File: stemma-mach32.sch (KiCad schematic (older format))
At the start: 28 parts, among them J1 Conn_01x09_Male, J2 Conn_01x04_Male, J3 Conn_01x04_Male, J4 Conn_01x09_Male, J5 DebugEdge_02x04, Q1 BSS138, Q2 BSS138, U1 AP2112K-3.3, U2 MACHXO2-32QFN

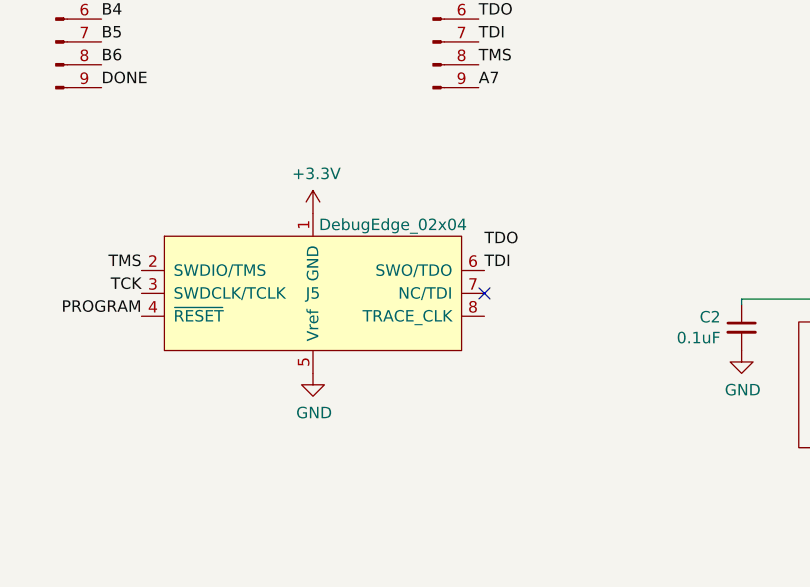
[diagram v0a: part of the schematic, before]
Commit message: fix: correct the FPGA package and DebugEdge schematic connections
Use the manufacturer's exact HC SG32 ordering and pinout data. Restore the schematic-to-PCB mapping broken by stale label placement around the pinned DebugEdge symbol, preserving copper and submodule revisions. Version the legacy symbol cache and retain all upstream licence scopes.
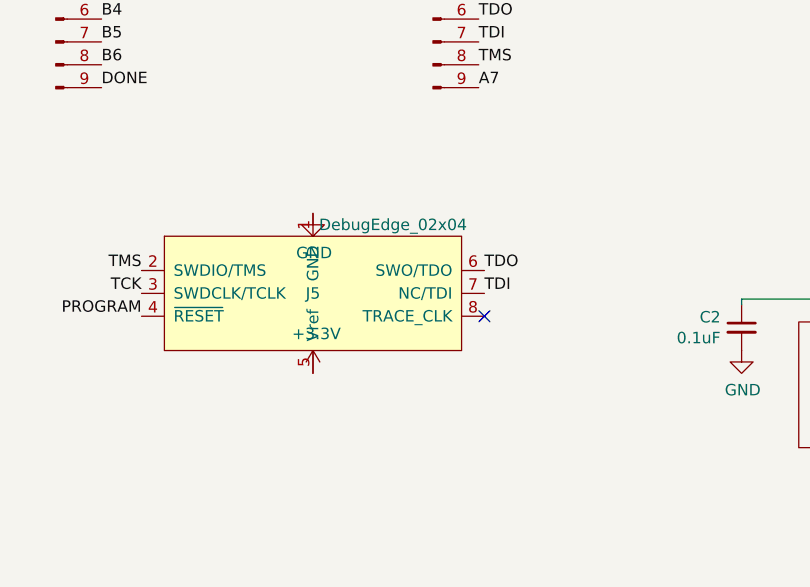
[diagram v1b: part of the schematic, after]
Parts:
- U2: Part # LCMXO2-1200HC-4MG132I -> LCMXO2-1200HC-4SG32I
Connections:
- net +3V3: now also J5.5 (Vref); no longer J5.1 (GND)
- net GND: now also J5.1 (GND); no longer J5.5 (Vref)
- net TDI: now also J5.7 (NC/TDI); no longer J5.6 (SWO/TDO)
- net TDO: now also J5.6 (SWO/TDO)
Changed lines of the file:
@@
 F 1 "MACHXO2-32QFN" H 5875 2650 50  0000 R CNN
 F 2 "Package_DFN_QFN:QFN-32-1EP_5x5mm_P0.5mm_EP3.1x3.1mm" H 5450 3375 50  0001 C CNN
-F 3 "http://www.latticesemi.com/~/media/LatticeSemi/Documents/DataSheets/MachXO23/MachXO2FamilyDataSheet.pdf" H 5450 3375 50  0001 C CNN
-F 4 "LCMXO2-1200HC-4MG132I" H 5450 3375 50  0001 C CNN "Part #"
+F 3 "https://www.latticesemi.com/view_document?document_id=38834" H 5450 3375 50  0001 C CNN
+F 4 "LCMXO2-1200HC-4SG32I" H 5450 3375 50  0001 C CNN "Part #"
 	1    5450 3375
 	1    0    0    -1
@@
 F 1 "MACHXO2-32QFN" H 8450 3025 50  0000 R CNN
 F 2 "Package_DFN_QFN:QFN-32-1EP_5x5mm_P0.5mm_EP3.1x3.1mm" H 8025 3425 50  0001 C CNN
-F 3 "http://www.latticesemi.com/~/media/LatticeSemi/Documents/DataSheets/MachXO23/MachXO2FamilyDataSheet.pdf" H 8025 3425 50  0001 C CNN
-F 4 "LCMXO2-1200HC-4MG132I" H 8025 3425 50  0001 C CNN "Part #"
+F 3 "https://www.latticesemi.com/view_document?document_id=38834" H 8025 3425 50  0001 C CNN
+F 4 "LCMXO2-1200HC-4SG32I" H 8025 3425 50  0001 C CNN "Part #"
 	2    8025 3425
 	1    0    0    -1
@@
 F 1 "MACHXO2-32QFN" H 7250 4625 50  0000 R CNN
 F 2 "Package_DFN_QFN:QFN-32-1EP_5x5mm_P0.5mm_EP3.1x3.1mm" H 6750 5150 50  0001 C CNN
-F 3 "http://www.latticesemi.com/~/media/LatticeSemi/Documents/DataSheets/MachXO23/MachXO2FamilyDataSheet.pdf" H 6750 5150 50  0001 C CNN
-F 4 "LCMXO2-1200HC-4MG132I" H 6750 5150 50  0001 C CNN "Part #"
+F 3 "https://www.latticesemi.com/view_document?document_id=38834" H 6750 5150 50  0001 C CNN
+F 4 "LCMXO2-1200HC-4SG32I" H 6750 5150 50  0001 C CNN "Part #"
 	3    6750 5150
 	1    0    0    -1
@@
 F 1 "MACHXO2-32QFN" H 4925 4475 50  0000 R CNN
 F 2 "Package_DFN_QFN:QFN-32-1EP_5x5mm_P0.5mm_EP3.1x3.1mm" H 4475 4900 50  0001 C CNN
-F 3 "http://www.latticesemi.com/~/media/LatticeSemi/Documents/DataSheets/MachXO23/MachXO2FamilyDataSheet.pdf" H 4475 4900 50  0001 C CNN
-F 4 "LCMXO2-1200HC-4MG132I" H 4475 4900 50  0001 C CNN "Part #"
+F 3 "https://www.latticesemi.com/view_document?document_id=38834" H 4475 4900 50  0001 C CNN
+F 4 "LCMXO2-1200HC-4SG32I" H 4475 4900 50  0001 C CNN "Part #"
 	4    4475 4900
 	1    0    0    -1
@@
 F 1 "MACHXO2-32QFN" H 9078 4905 50  0000 L CNN
 F 2 "Package_DFN_QFN:QFN-32-1EP_5x5mm_P0.5mm_EP3.1x3.1mm" H 8900 4925 50  0001 C CNN
-F 3 "http://www.latticesemi.com/~/media/LatticeSemi/Documents/DataSheets/MachXO23/MachXO2FamilyDataSheet.pdf" H 8900 4925 50  0001 C CNN
-F 4 "LCMXO2-1200HC-4MG132I" H 8900 4925 50  0001 C CNN "Part #"
+F 3 "https://www.latticesemi.com/view_document?document_id=38834" H 8900 4925 50  0001 C CNN
+F 4 "LCMXO2-1200HC-4SG32I" H 8900 4925 50  0001 C CNN "Part #"
 	5    8900 4925
 	1    0    0    -1
@@
 L power:+3.3V #PWR0131
 U 1 1 5F6520D1
-P 2150 4225
-F 0 "#PWR0131" H 2150 4075 50  0001 C CNN
-F 1 "+3.3V" H 2165 4398 50  0000 C CNN
-F 2 "" H 2150 4225 50  0001 C CNN
-F 3 "" H 2150 4225 50  0001 C CNN
-	1    2150 4225
+P 2150 4925
+F 0 "#PWR0131" H 2150 4775 50  0001 C CNN
+F 1 "+3.3V" H 2165 5098 50  0000 C CNN
+F 2 "" H 2150 4925 50  0001 C CNN
+F 3 "" H 2150 4925 50  0001 C CNN
+	1    2150 4925
 	1    0    0    -1
 $EndComp
 Text Label 1400 4675 2    50   ~ 0
 PROGRAM
-NoConn ~ 2900 4575
-Text Label 2900 4375 0    50   ~ 0
+NoConn ~ 2900 4675
+Text Label 2900 4475 0    50   ~ 0
 TDO
-Text Label 2900 4475 0    50   ~ 0
+Text Label 2900 4575 0    50   ~ 0
 TDI
 Text Label 1400 4475 2    50   ~ 0
@@
 L power:GND #PWR0133
 U 1 1 5F59913B
-P 2150 4925
-F 0 "#PWR0133" H 2150 4675 50  0001 C CNN
-F 1 "GND" H 2155 4752 50  0000 C CNN
-F 2 "" H 2150 4925 50  0001 C CNN
-F 3 "" H 2150 4925 50  0001 C CNN
-	1    2150 4925
-	1    0    0    -1
-$EndComp
+P 2150 4225
+F 0 "#PWR0133" H 2150 3975 50  0001 C CNN
+F 1 "GND" H 2155 4052 50  0000 C CNN
+F 2 "" H 2150 4225 50  0001 C CNN
+F 3 "" H 2150 4225 50  0001 C CNN
+	1    2150 4225
+	1    0    0    -1
+$EndComp
